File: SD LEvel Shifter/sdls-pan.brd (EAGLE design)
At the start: 30 x 25 mm, 8 parts

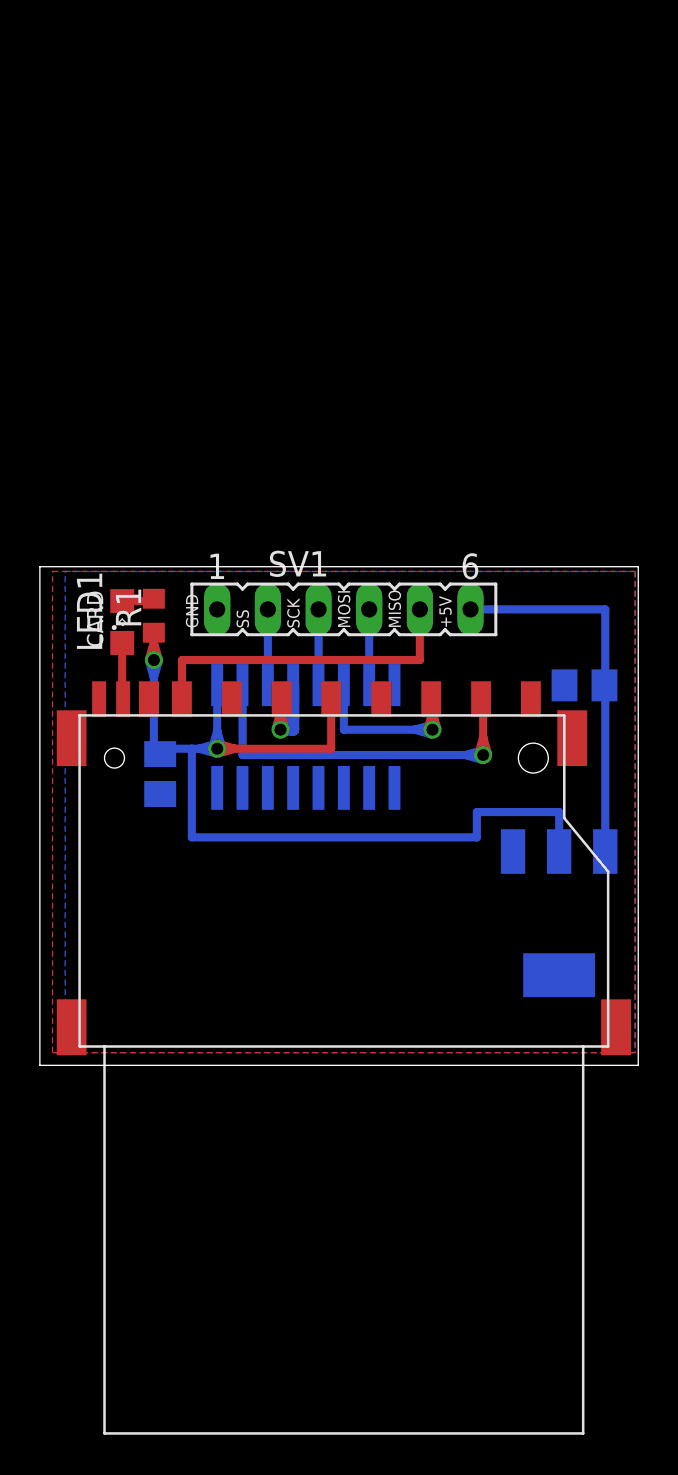
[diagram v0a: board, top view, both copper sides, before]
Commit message: panelized level shifter, ran gerber export
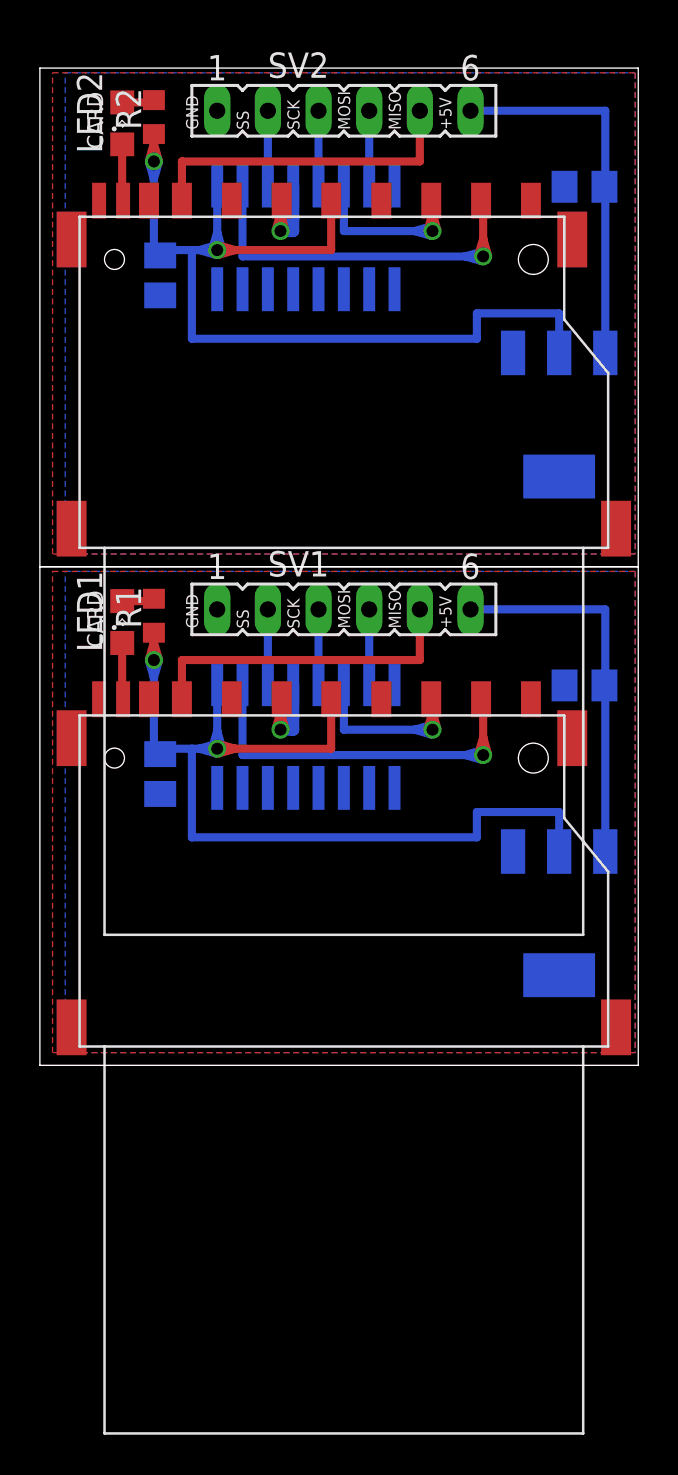
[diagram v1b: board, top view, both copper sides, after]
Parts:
- added C3, C4: (no value), rcl:C0805K
- added IC2: (no value), SparkFun:SOT223
- added LED2: (no value), led:SML0805
- added R2: (no value), rcl:R0603
- added SV2: (no value), con-lsta:FE06
- added U$2: SD_CARD, tbsliver-con-memory:MEM1055
- added U2: (no value), microbuilder:SOIC16
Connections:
- new net +3V1: C4.1, IC2.2, R2.1, U$2.P4, U2.1
- new net +5V1: C3.1, IC2.3, SV2.6
- new net GND1: C3.2, C4.2, IC2.1, SV2.1, U$2.P3, U$2.P6, U$2.SHIELD0, U$2.SHIELD1, U$2.SHIELD2, U$2.SHIELD3, U$2.WP, U2.8
- new net MISO1: SV2.5, U$2.P7
- new net MOSI1: SV2.4, U2.7
- new net N$3: LED2.C, U$2.CD
- new net N$4: LED2.A, R2.2
- new net SCK1: SV2.3, U2.5
- new net SS1: SV2.2, U2.3
- new net S_MOSI1: U$2.P2, U2.6
- new net S_SCK1: U$2.P5, U2.4
- new net S_SS1: U$2.P1, U2.2
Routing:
- net +3V1: track 0.00 -> 57.9 mm, vias 0 -> 2
- net S_SS1: track 0.00 -> 23.0 mm, vias 0 -> 1
- net +5V1: track 0.00 -> 18.9 mm
- net MISO1: track 0.00 -> 16.4 mm
- net S_MOSI1: track 0.00 -> 12.8 mm, vias 0 -> 1
- net S_SCK1: track 0.00 -> 8.80 mm, vias 0 -> 1
- net SS1: track 0.00 -> 3.75 mm
- net SCK1: track 0.00 -> 3.75 mm
- net MOSI1: track 0.00 -> 3.75 mm
- net N$3: track 0.00 -> 2.86 mm
- net N$4: track 0.00 -> 1.70 mm
- added copper zone on layer 1, net GND1
- added copper zone on layer 16, net GND1
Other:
- board size 30 x 25 mm -> 30 x 50 mm
